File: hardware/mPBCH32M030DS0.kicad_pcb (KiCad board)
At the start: 2 copper layers, 60 x 42 mm, 100 parts, among them J1 PWR_IN, J10 B2B_SIG, J3 HALL, J4 I2C, J5 UART, J6 GPIO, J7 SDI, J8 USB-C, J9 B2B_PWR, Q10 TPN1R603PL, Q9 TPN2R304PL, SW1 RESET, SW2 USER/BOOT, U1 CH32M030C8U7, U2 78L05, U3 USBLC6-2SC6, U4 LM74700-Q1, U5 LM74700-Q1, Y1 8MHz CL=20pF

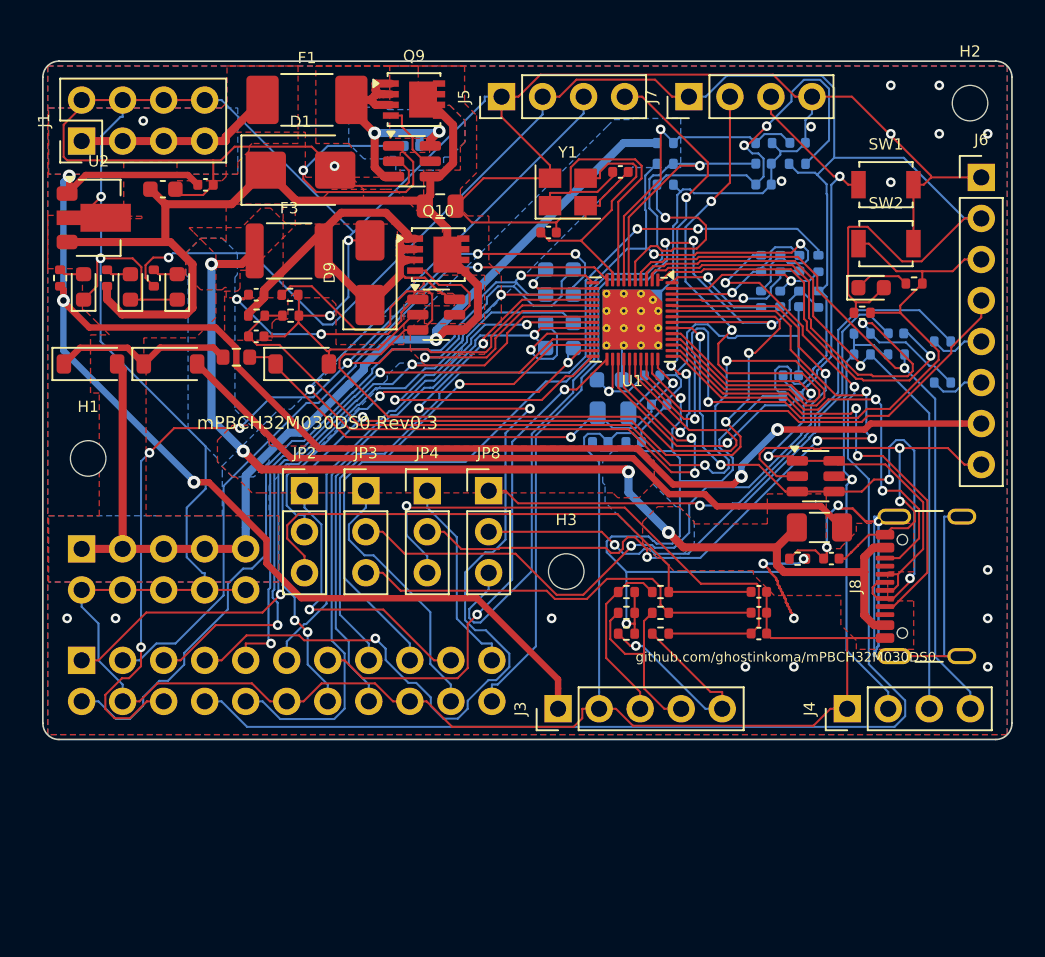
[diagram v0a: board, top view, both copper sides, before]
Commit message: Rev 0.4: DIP-42 MCU module + power boards A/B/C (KiCad 8)
- MCU module: 20.32 x 53.34mm (8 x 21 grid), DIP-42 (0.6in rows), fits
  an 82 x 52mm breadboard. Headers can be fitted from either side;
  signal names on bottom silk. All LEDs (power, status, 8 gate LEDs) on
  the module top.
- Power boards take the module in two 1x21 sockets (left/right
  symmetric mating). FETs/shunts on the heatsink side, no LEDs.
  Voltage-dependent parts (TVS, OVP divider, bulk caps, BEMF divider)
  moved to the power boards. Breakout board D removed.
  A/C: 20.32 x 71.94mm, B (TO-263 x8): 40.64 x 66.94mm.
- Capacitors re-selected for realistic size vs voltage/capacitance
  (4.7uF 1608, 10uF/25V 2012, 10uF/50V 1206, 4.7nF/100V 1608, low
  profile electrolytics).
- Schematics and boards generated in KiCad 8 format; netlists verified
  with KiCad 8.0.9.
- Layout pipeline: Freerouting bridge (parallel), second pass, early
  repair before pours, island-aware maze repair, DRC via kicad-cli.
- DRC: power boards A/B/C have 0 unconnected / 0 electrical errors.
  The MCU module still has unrouted connections (work in progress).

Co-Authored-By: Claude Opus 5.5 <noreply@anthropic.com>
Claude-Session: https://claude.ai/code/session_01LENFjjhDfYjJZV1NWhB9uV
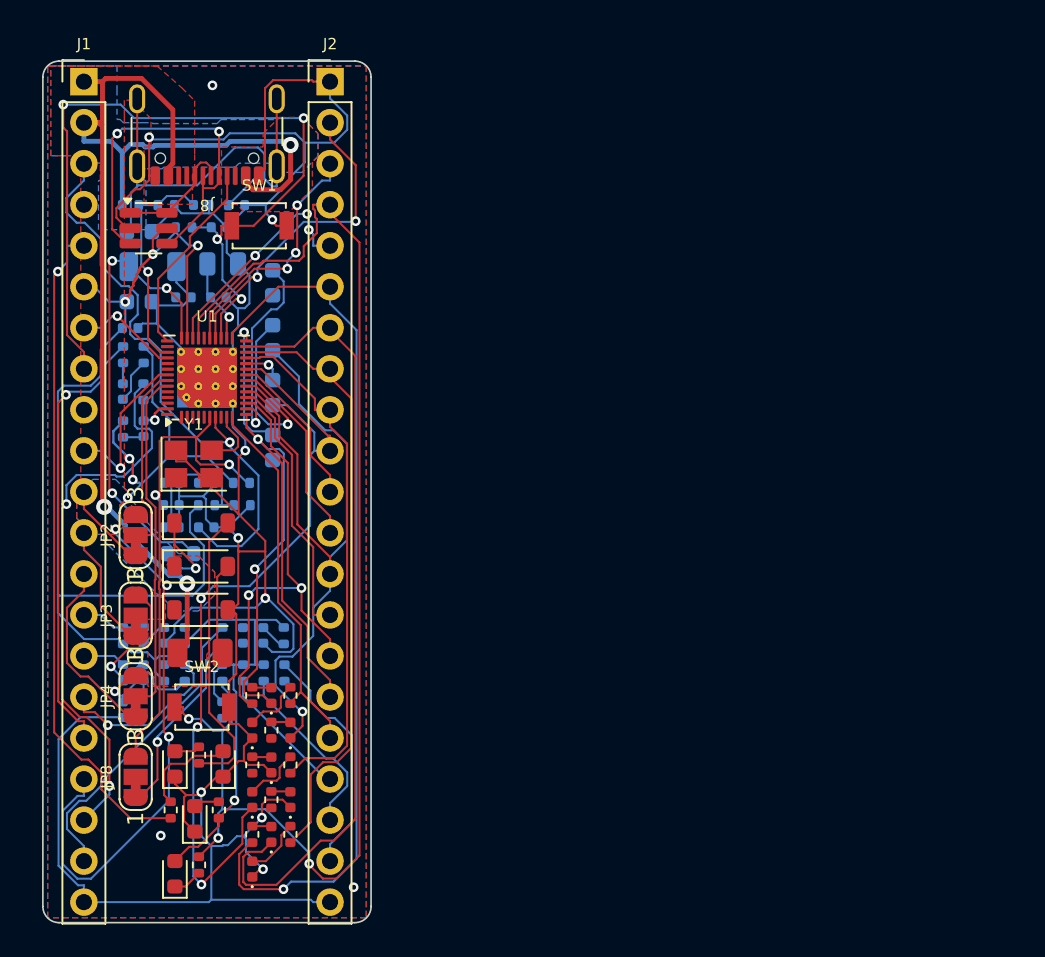
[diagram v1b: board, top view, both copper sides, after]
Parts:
- removed C1: 10uF/50V, C_0805_2012Metric
- removed C3: 1uF/50V, C_0603_1608Metric
- removed C4: 1uF/25V, C_0402_1005Metric
- removed C5, C6: 0.1uF/50V, C_0402_1005Metric
- removed D1: SMBJ16A, D_SMB
- removed D9: SMAJ20A, D_SMA
- removed F1: 10A, Fuse_Littelfuse_NANO2_2410
- removed F3: 5A, Fuse_1812_4532Metric
- removed H1, H2, H3: M2, MountingHole_2.2mm_M2
- removed J10: B2B_SIG, PinHeader_2x11_P2.54mm_Vertical
- removed J3: HALL, PinHeader_1x05_P2.54mm_Vertical
- removed J4: I2C, PinHeader_1x04_P2.54mm_Vertical
- removed J5: UART, PinHeader_1x04_P2.54mm_Vertical
- removed J6: GPIO, PinHeader_1x08_P2.54mm_Vertical
- removed J7: SDI, PinHeader_1x04_P2.54mm_Vertical
- removed J9: B2B_PWR, PinHeader_2x05_P2.54mm_Vertical
- removed Q10: TPN1R603PL, Vishay_PowerPAK_1212-8_Single
- removed Q9: TPN2R304PL, Vishay_PowerPAK_1212-8_Single
- removed R11: 110k 1%, R_0402_1005Metric
- removed R12: 10k 1%, R_0402_1005Metric
- removed R6: 100k, R_0402_1005Metric
- removed U2: 78L05, SOT-89-3
- removed U4, U5: LM74700-Q1, SOT-23-6
- added D10: RED GH0, LED_0402_1005Metric, F.Cu at (14.1, 39.3)
- added D11: GREEN GL0, LED_0402_1005Metric, F.Cu at (13.0, 41.4)
- added D12: RED GH1, LED_0402_1005Metric, F.Cu at (15.3, 41.4)
- added D13: GREEN GL1, LED_0402_1005Metric, F.Cu at (14.1, 43.6)
- added D14: RED GH2, LED_0402_1005Metric, F.Cu at (13.0, 45.7)
- added D15: GREEN GL2, LED_0402_1005Metric, F.Cu at (15.3, 45.7)
- added D16: RED GH3, LED_0402_1005Metric, F.Cu at (14.1, 47.9)
- added D17: GREEN GL3, LED_0402_1005Metric, F.Cu at (13.0, 50.0)
- added J2: EDGE_R, PinHeader_1x21_P2.54mm_Vertical, F.Cu at (17.8, 1.27)
- added R50: 22k, R_0402_1005Metric, F.Cu at (13.0, 39.3)
- added R51: 22k, R_0402_1005Metric, F.Cu at (15.3, 39.3)
- added R52: 22k, R_0402_1005Metric, F.Cu at (14.1, 41.4)
- added R53: 22k, R_0402_1005Metric, F.Cu at (13.0, 43.6)
- added R54: 22k, R_0402_1005Metric, F.Cu at (15.3, 43.6)
- added R55: 22k, R_0402_1005Metric, F.Cu at (14.1, 45.7)
- added R56: 22k, R_0402_1005Metric, F.Cu at (13.0, 47.9)
- added R57: 22k, R_0402_1005Metric, F.Cu at (15.3, 47.9)
- C10: footprint C_0805_2012Metric -> C_1206_3216Metric
- C100, C101, C102, C131, C132, C7, R10, R100, R101, R103, R104, R106, R107, R111, R130, R7, R8: moved to B.Cu
- C12: footprint C_0603_1608Metric -> C_0805_2012Metric
- C130: footprint C_0402_1005Metric -> C_0603_1608Metric; moved to B.Cu
- C14: value 4.7uF/10V -> 4.7uF/16V; footprint C_0402_1005Metric -> C_0603_1608Metric
- J1: value PWR_IN -> EDGE_L; footprint PinHeader_2x04_P2.54mm_Vertical -> PinHeader_1x21_P2.54mm_Vertical
- JP2, JP3, JP4, JP8: footprint PinHeader_1x03_P2.54mm_Vertical -> SolderJumper-3_P1.3mm_Bridged12_RoundedPad1.0x1.5mm_NumberLabels
- moved R112 57.1 mm to (9.66, 49.8), turned to 90 degrees
- moved D3 56.3 mm to (8.18, 50.3), turned to 90 degrees
- moved J8 54.2 mm to (10.2, 3.41), turned to 180 degrees
- moved SW2 51.2 mm to (9.85, 40.0)
- moved R123 48.2 mm to (11.1, 35.6), turned to -90 degrees
- moved C130 47.4 mm to (5.97, 10.6)
- moved R122 46.0 mm to (11.1, 40.2), turned to -90 degrees
- moved R111 45.5 mm to (11.1, 37.9), turned to -90 degrees
- moved C105 44.5 mm to (12.4, 35.6), turned to -90 degrees
- moved R120 44.5 mm to (15.0, 37.9), turned to -90 degrees
- moved U3 44.1 mm to (6.54, 10.3)
- moved R115 43.8 mm to (13.7, 37.9), turned to -90 degrees
- moved C16 43.7 mm to (10.1, 28.9)
- moved R114 43.1 mm to (12.4, 37.9), turned to -90 degrees
- moved C19 42.6 mm to (4.96, 20.5)
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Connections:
- net LED5_A renamed LED_D2_A
- J1 pad 1: VIN -> USB_VBUS
- J1 pad 2: GND -> USB_VBUS
- J1 pad 3: VIN -> VBUS_SNS
- J1 pad 4: GND -> PD_PWR_EN
- J1 pad 5: VIN -> +5V
- J1 pad 6: GND -> +3V3
- J1 pad 7: VIN -> SWDIO
- J1 pad 8: GND -> nRST
- R7 pad 1: USB_VBUS_P -> USB_VBUS
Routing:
- net GND: track 404.5 -> 209.9 mm, vias 26 -> 11
- net VBUS: track 119.8 -> 18.0 mm, vias 1 -> 0
- net +3V3: track 194.2 -> 95.8 mm
- net +5V: track 127.8 -> 41.5 mm, vias 5 -> 1
- net PD_PWR_EN: track 57.3 -> 0.00 mm
- net ISA_SEL: track 80.2 -> 27.6 mm, vias 2 -> 1
- net SENS_V: track 50.2 -> 0.00 mm, vias 2 -> 0
- net USB_VBUS_SNS: track 62.0 -> 13.9 mm, vias 2 -> 1
- net LO1: track 64.2 -> 16.5 mm, vias 4 -> 0
- net NTC: track 55.4 -> 11.7 mm, vias 3 -> 1
- net UART_TX: track 60.7 -> 19.7 mm, vias 3 -> 2
- net SENS_U: track 51.6 -> 11.6 mm, vias 3 -> 0
- net USB_VBUS_F: track 44.1 -> 5.76 mm
- net QII_SRC: track 34.9 -> 0.00 mm, vias 1 -> 0
- net I2C_SDA: track 42.5 -> 8.45 mm, vias 1 -> 0
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- removed copper zone on F.Cu, net USB_VBUS_P
- removed copper zone on B.Cu, net VBUS
- removed copper zone on F.Cu, net VBUS
- removed copper zone on B.Cu, net VIN
- removed copper zone on F.Cu, net VIN
- removed copper zone on B.Cu, net VIN_F
- removed copper zone on F.Cu, net VIN_F
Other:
- board size 60 x 42 mm -> 20.3 x 53.3 mm
- board text added: "+3V3"
- board text added: "+5V"
- board text added: "BEMF_U"
- board text added: "BEMF_V"
- board text added: "BEMF_W"
- board text added: "GND"
- board text added: "GPIO_PC4"
- board text added: "GPIO_PC5"
- board text added: "HALL_A"
- board text added: "HALL_B"
- board text added: "HALL_C"
- board text added: "HO0"
- board text added: "HO1"
- board text added: "HO2"
- board text added: "HO3"
- board text added: "I2C_SCL"
- board text added: "I2C_SDA"
- board text added: "ISA_SEL"
- board text added: "ISB_SEL"
- board text added: "ISH"
- board text added: "LO0"
- board text added: "LO1"
- board text added: "LO2"
- board text added: "LO3"
- board text added: "NTC"
- board text added: "PD_PWR_EN"
- board text added: "SW0"
- board text added: "SW1"
- board text added: "SW2"
- board text added: "SW3"
- board text added: "SWDIO"
- board text added: "TACH"
- board text added: "UART_RX"
- board text added: "UART_TX"
- board text added: "UVBUS"
- board text added: "VBUS"
- board text added: "VBUS_SNS"
- board text added: "ghostinkoma/mPBCH32M030DS0"
- board text added: "mPB CH32M030"
- board text added: "nFAULT"
- board text added: "nRST"
- board text removed: "github.com/ghostinkoma/mPBCH32M030DS0"
- board text removed: "mPBCH32M030DS0 Rev0.3"

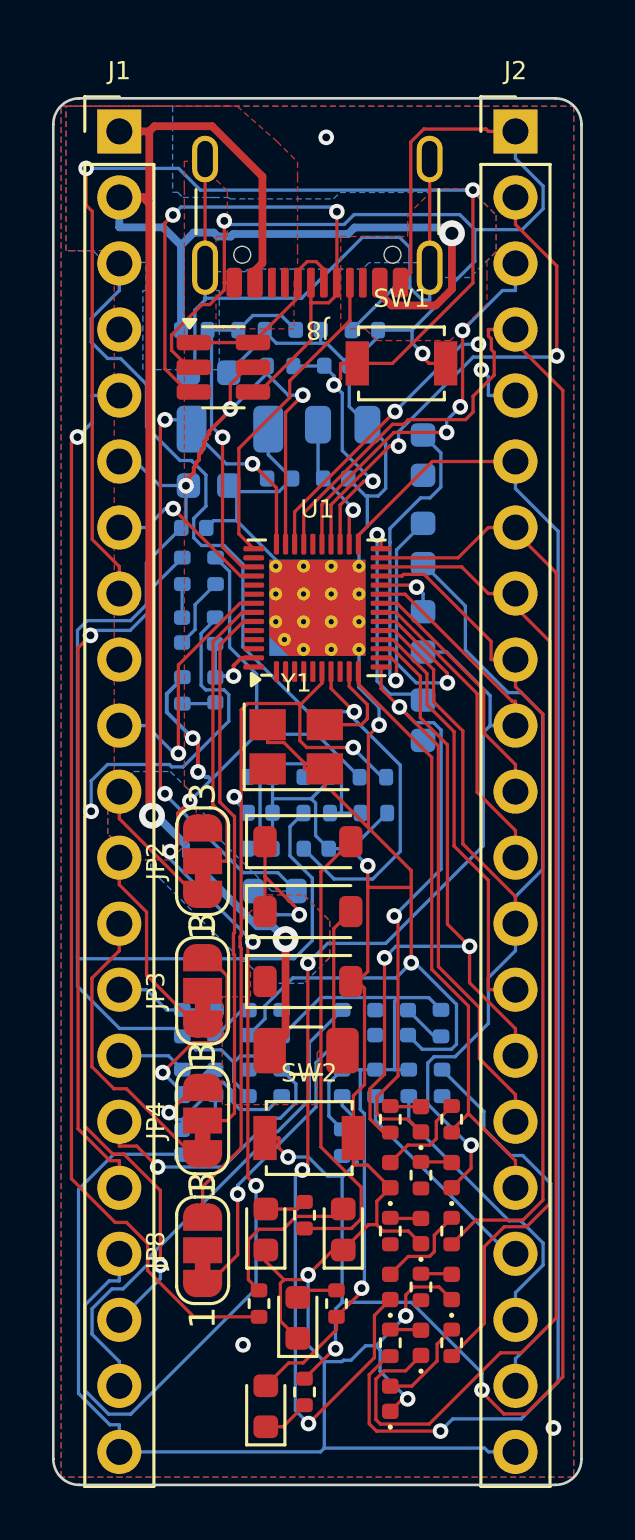
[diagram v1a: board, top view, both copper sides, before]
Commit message: Rev 0.4: rework module pinout for routability, power boards regenerated
- Module edge pin order follows the CH32M030 QFN48 pin sides so the
  breakout traces nest instead of crossing (J1: USB_VBUS, PD_PWR_EN,
  PC4/PC5, +3V3, +5V, SWDIO, VBUS, NTC, BEMF, HALL, ISx, TACH;
  J2: RX/TX, nRST, gate drive HO3..LO0, VBUS_SNS, I2C, nFAULT).
- Module: area under the QFN kept for fan-out (filters and the VHV/USB
  diode block moved away, gate LEDs right-aligned to J2).
- Power boards A/B/C re-placed for the new pinout (VBUS divider next to
  J2 VBUS_SNS, LM74700 next to its FET) and re-routed: all three at
  0 unconnected / 0 electrical DRC errors.
- Layout tooling: DRC via kicad-cli in a separate process, reload after
  SES import, selectable Freerouting jar, optional rip-up repair,
  configurable Freerouting timeout.
- MCU module still has unrouted connections (work in progress).

Co-Authored-By: Claude Opus 5.5 <noreply@anthropic.com>
Claude-Session: https://claude.ai/code/session_01LENFjjhDfYjJZV1NWhB9uV
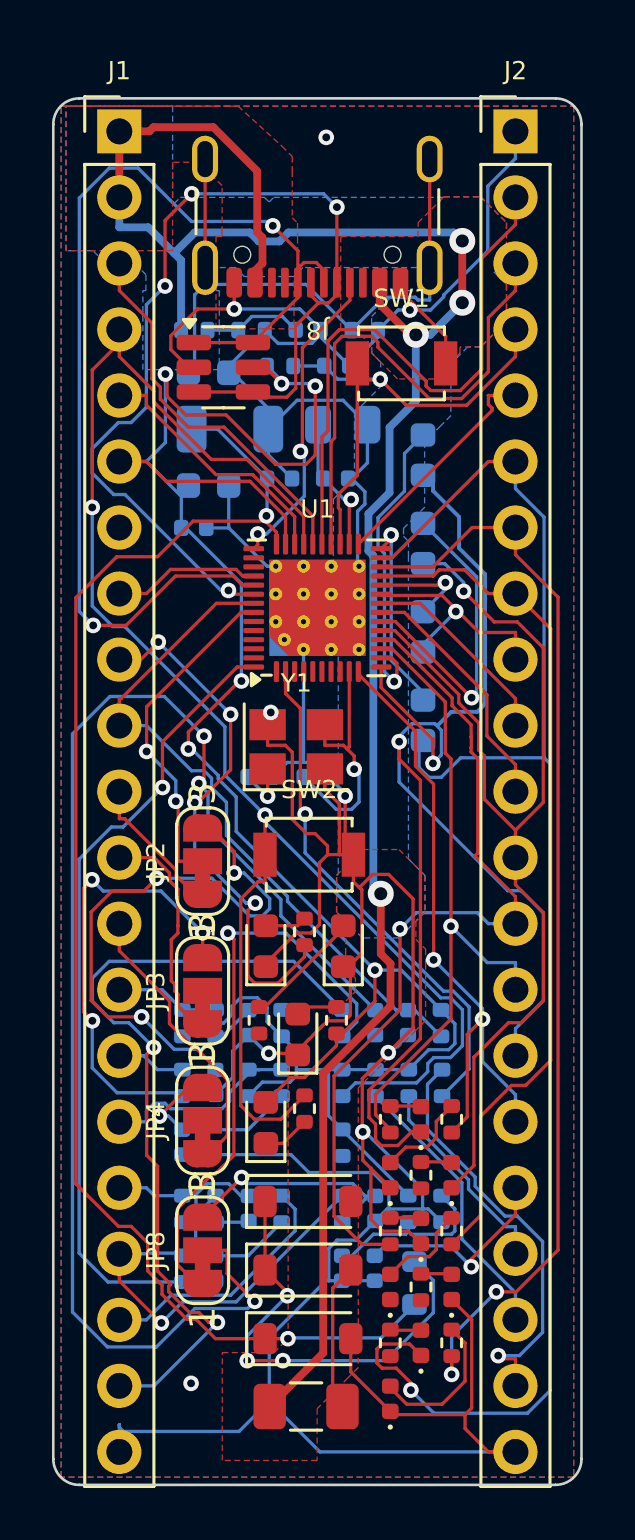
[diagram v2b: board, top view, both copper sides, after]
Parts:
- moved R16 24.6 mm to (4.96, 42.7)
- moved R17 24.6 mm to (6.25, 42.7)
- moved C19 22.4 mm to (7.51, 42.7)
- moved R18 22.4 mm to (8.79, 42.7)
- moved C20 22.3 mm to (6.24, 45.0)
- moved R19 22.2 mm to (4.96, 45.0)
- moved R13 16.7 mm to (11.1, 42.7), turned to -90 degrees
- moved C18 16.4 mm to (11.1, 45.0), turned to -90 degrees
- moved C16 16.3 mm to (12.4, 45.0), turned to -90 degrees
- moved R10 16.0 mm to (13.9, 45.6), turned to -90 degrees
- moved C17 15.9 mm to (12.4, 42.7), turned to -90 degrees
- moved R14 15.6 mm to (13.7, 42.7), turned to -90 degrees
- moved R15 15.5 mm to (14.9, 42.7), turned to -90 degrees
- moved D5 13.8 mm to (9.79, 42.4)
- moved D6 13.8 mm to (9.79, 45.1)
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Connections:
- J1 pad 3: VBUS_SNS -> PD_PWR_EN
- J1 pad 4: PD_PWR_EN -> GPIO_PC4
- J1 pad 5: +5V -> GPIO_PC5
- J1 pad 7: SWDIO -> +5V
- J1 pad 8: nRST -> SWDIO
- J2 pad 10: SW2 -> LO2
- J2 pad 11: LO2 -> HO1
- J2 pad 12: HO1 -> SW1
- J2 pad 13: SW1 -> LO1
- J2 pad 14: LO1 -> HO0
- J2 pad 15: HO0 -> SW0
- J2 pad 16: SW0 -> LO0
- J2 pad 17: LO0 -> VBUS_SNS
- J2 pad 18: I2C_SDA -> I2C_SCL
- J2 pad 19: I2C_SCL -> I2C_SDA
- J2 pad 2: UART_TX -> UART_RX
- J2 pad 3: UART_RX -> UART_TX
- J2 pad 4: GPIO_PC4 -> nRST
- J2 pad 5: GPIO_PC5 -> HO3
- J2 pad 6: HO3 -> SW3
- J2 pad 7: SW3 -> LO3
- J2 pad 8: LO3 -> HO2
- J2 pad 9: HO2 -> SW2
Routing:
- net QII_SRC: track 0.00 -> 53.6 mm, vias 0 -> 3
- net HO3: track 54.8 -> 8.96 mm, vias 1 -> 0
- net SW2: track 50.8 -> 8.99 mm, vias 3 -> 1
- net +5V: track 41.5 -> 0.00 mm, vias 1 -> 0
- net ISH: track 56.1 -> 17.6 mm, vias 6 -> 1
- net USB_DP: track 7.54 -> 42.3 mm, vias 0 -> 2
- net nRST: track 52.5 -> 19.2 mm, vias 4 -> 1
- net IB_N: track 1.29 -> 31.7 mm, vias 0 -> 1
- net VBUS_SNS: track 37.1 -> 7.94 mm
- net ISA_SEL: track 27.6 -> 2.55 mm, vias 1 -> 0
- net VHV: track 29.5 -> 54.4 mm, vias 3 -> 2
- net ISB_SEL: track 34.3 -> 9.74 mm, vias 2 -> 0
- net HALL_A: track 1.69 -> 23.6 mm, vias 0 -> 3
- net IBUS_F: track 30.6 -> 8.93 mm, vias 2 -> 1
- net SENS_W: track 21.3 -> 0.00 mm
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
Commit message: 8マス版 MCU モジュールの配線を完成 (未接続 0)
- 水晶 Y1 と C131/C132 を XI/XO 直下の裏面へ移す配置を 8 マス版にも適用
- 8 マス版モジュールのみ線幅・間隙 0.10mm / ビア 0.5mm (穴 0.25mm) に詰める
  (0.127mm では 5 通りの試行とも未接続 19〜27 が残ったため)。MPB_RULE / MPB_VIA で上書き可
- DRC: 未接続 0 / 電気的エラー 0 (シルク警告のみ)
- ベタなし版 (w8_nopour)、製造データ、図、DRC まとめを再生成
- README / stacking.md を更新 (両版とも配線完了)

Co-Authored-By: Claude Opus 5.5 <noreply@anthropic.com>
Claude-Session: https://claude.ai/code/session_01LENFjjhDfYjJZV1NWhB9uV
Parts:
- Y1: moved to B.Cu
- moved C132 2.66 mm to (9.97, 28.8)
- moved C131 2.40 mm to (9.97, 27.4)
- moved Y1 1.48 mm to (10.8, 24.5), turned to -90 degrees
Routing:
- net I2C_SCL: track 7.98 -> 70.0 mm, vias 0 -> 8
- net I2C_SDA: track 10.8 -> 57.7 mm, vias 0 -> 2
- net HO3: track 8.96 -> 51.9 mm
- net QII_SRC: track 53.6 -> 18.8 mm, vias 3 -> 1
- net IA_N: track 1.29 -> 32.4 mm, vias 0 -> 3
- net IB_P: track 3.08 -> 33.6 mm, vias 0 -> 1
- net SW2: track 8.99 -> 38.9 mm
- net OCP_REF: track 6.75 -> 36.2 mm, vias 0 -> 1
- net IA_P: track 3.68 -> 31.5 mm, vias 0 -> 1
- net LO2: track 7.73 -> 34.9 mm
- net VHV: track 54.4 -> 80.5 mm, vias 2 -> 4
- net VBUS: track 21.6 -> 46.9 mm, vias 4 -> 3
- net VBUS_SNS: track 7.94 -> 33.2 mm, vias 1 -> 4
- net SENS_W: track 0.00 -> 24.5 mm, vias 0 -> 2
- net nFAULT: track 19.9 -> 44.1 mm, vias 1 -> 4
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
